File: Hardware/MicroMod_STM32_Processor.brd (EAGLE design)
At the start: 22 x 22 mm, 44 parts, among them J1 MICROMOD-2222, U1 STM32F405RGT6, U3 W25QXX128MBIT-6X5, Y1 12MHz, Y2 32.768kHz

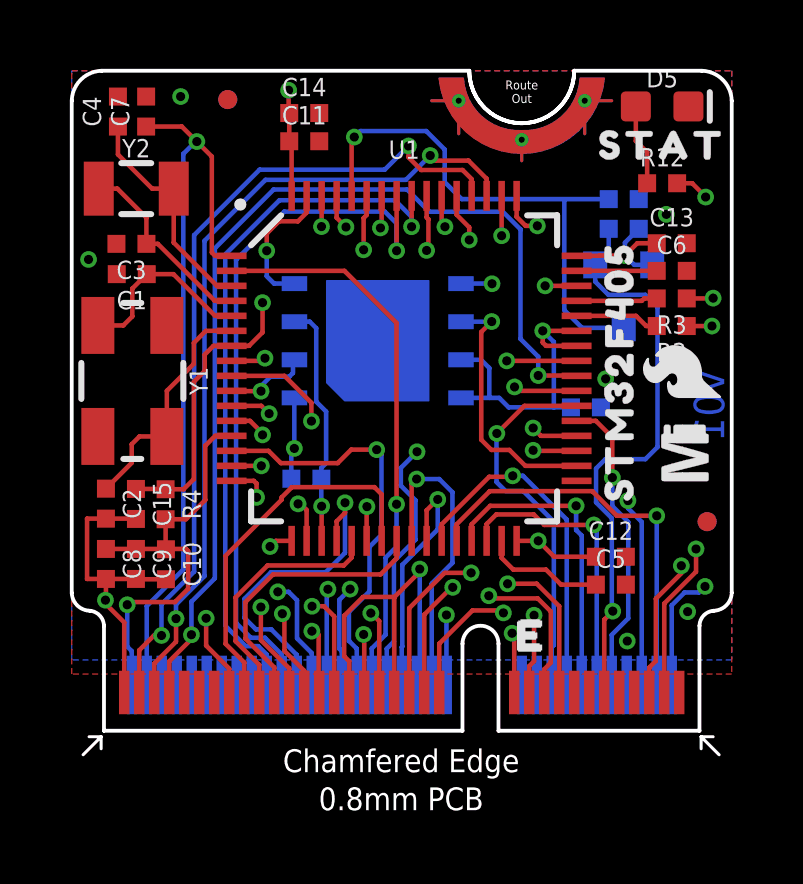
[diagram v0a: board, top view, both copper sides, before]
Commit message: V01 Update
Added jumper for USB host config
Updated crystal caps
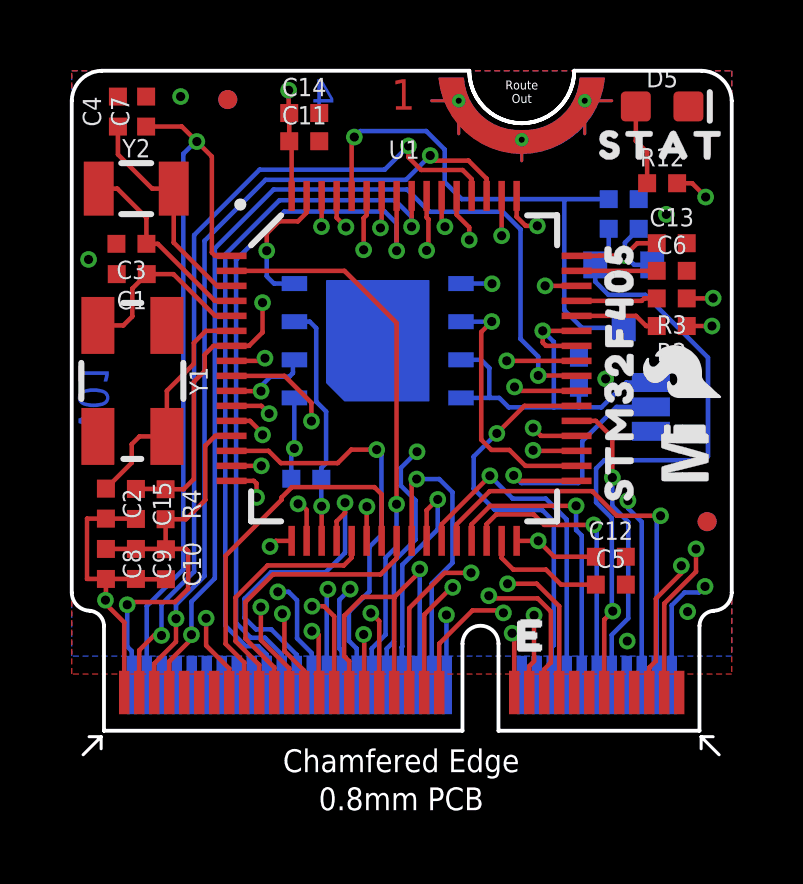
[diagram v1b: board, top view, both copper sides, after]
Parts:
- added HOST_ID: (no value), SparkFun-Jumpers:SMT-JUMPER_3_NO_NO-SILK
- C3, C4: value 22pF -> 15pF
- moved C20 1.18 mm to (16.9, 11.9), turned to 90 degrees
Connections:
- net 3.3V: now also HOST_ID.1
- net GND: now also HOST_ID.3
- net HOST_ID: now also HOST_ID.2
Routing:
- net HOST_ID: track 0.00 -> 8.65 mm, vias 0 -> 1
- net 3.3V: track 49.4 -> 53.1 mm
- net !BOOT: track 19.2 -> 21.8 mm
- net D1: track 12.6 -> 13.8 mm
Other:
- board text added: "1"
- board text added: "2"
- board text added: "3"
- board text added: "4"

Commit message: The 'ol pin switch-a-roo
- Swapped D0/D1 with PWM0/1 - PWM pins weren't capable of PWM
- Swapped BATT_VIN with STAT - BATT_VIN needs to be on an ADC pin
- Moved PB13 to G10 - Based on testing VBUS needs to be broken out or pulled high for USB HS/FS to work correctly
- Moved PB12 from jumper to G11 for USB Host ID to match with SAMD51 MM
- Reorganized G0-G6 for better routing
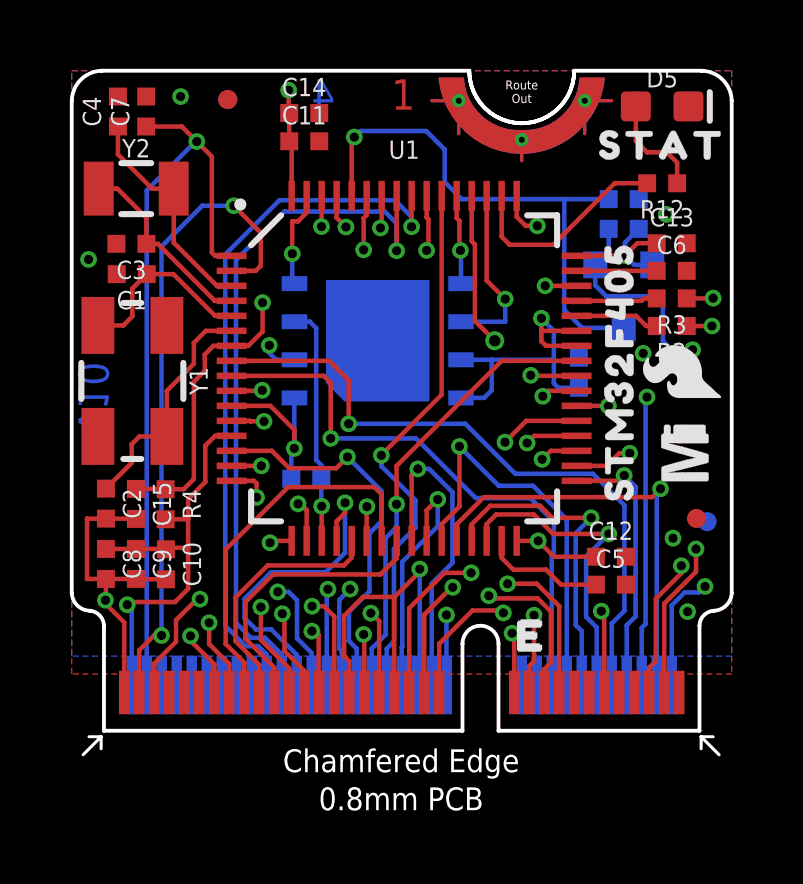
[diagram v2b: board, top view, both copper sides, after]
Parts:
- removed HOST_ID: (no value), SparkFun-Jumpers:SMT-JUMPER_3_NO_NO-SILK
- moved FD1 0.37 mm to (20.8, 7.08)
- moved U$5 0.10 mm to (5.16, 6.36)
- moved U$2 0.07 mm to (12.2, 6.36)
- turned R12 to 180 degrees
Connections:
- removed net G7: J1.69, U1.40
- new net HOST_VBUS: J1.63, U1.34
- net 3.3V: no longer HOST_ID.1
- net BATT_VIN: now also U1.15; no longer U1.50
- net D0: now also U1.8; no longer U1.37
- net D1: now also U1.9; no longer U1.38
- net FLASH_!CS: now also U1.11; no longer U1.39
- net FLASH_SCK: now also U1.51; no longer U1.34
- net FLASH_SDI: now also U1.53; no longer U1.11
- net FLASH_SDO: now also U1.52; no longer U1.10
- net G0: now also U1.54; no longer U1.41
- net G1: now also U1.41; no longer U1.2
- net G3: now also U1.39; no longer U1.53
- net G4: now also U1.40; no longer U1.54
- net G5: now also U1.2; no longer U1.52
- net G6: now also U1.10; no longer U1.51
- net GND: no longer HOST_ID.3
- net HOST_ID: now also J1.8; no longer HOST_ID.2
- net PWM0: now also U1.37; no longer U1.8
- net PWM1: now also U1.38; no longer U1.9
- net STAT: now also U1.50; no longer U1.15
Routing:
- net HOST_VBUS: track 0.00 -> 41.9 mm, vias 0 -> 2
- net G7: track 33.4 -> 0.00 mm, vias 2 -> 0
- net BATT_VIN: track 36.4 -> 14.8 mm
- net STAT: track 23.3 -> 7.17 mm, vias 2 -> 0
- net G6: track 27.2 -> 13.3 mm
- net D0: track 10.1 -> 22.1 mm
- net G3: track 26.3 -> 14.7 mm
- net FLASH_SDI: track 14.3 -> 2.99 mm, vias 2 -> 1
- net FLASH_SDO: track 2.86 -> 13.9 mm, vias 1 -> 2
- net G4: track 25.5 -> 15.5 mm
- net FLASH_!CS: track 13.1 -> 5.78 mm, vias 2 -> 1
- net PWM0: track 18.6 -> 11.8 mm
- net G5: track 27.9 -> 21.7 mm
- net D1: track 13.8 -> 19.3 mm
- net SWCLK: track 22.5 -> 18.2 mm
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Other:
- board text added: "v10"
- board text removed: "v01"

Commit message: V10 design review changes
Removed battery and 3.3V_EN connections to MicroMod
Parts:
- removed C7: 0.1uF, SparkFun-Capacitors:0402-TIGHT
- C15, C8: device SparkFun-Capacitors:0402-TIGHT -> SparkFun-Capacitors:0402
- moved C4 0.82 mm to (1.99, 20.0), turned to 180 degrees
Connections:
- removed net 3V3_EN: J1.4, U1.28
- removed net V_BATT: C7.1, J1.72, U1.1
- net GND: now also U1.28; no longer C7.2
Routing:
- net V_BATT: track 25.4 -> 0.00 mm, vias 1 -> 0
- net 3V3_EN: track 14.4 -> 0.00 mm, vias 1 -> 0
- net G5: track 21.7 -> 18.1 mm
- net GND: track 33.3 -> 35.3 mm
- net BOOT0: track 18.1 -> 17.0 mm
- net D1: track 19.3 -> 18.4 mm
- net D0: track 22.1 -> 21.3 mm
- net A0: track 10.7 -> 9.98 mm
- net N$5: track 7.59 -> 6.91 mm

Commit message: Double-check changes
- Added VDD range
- Updated 0.1uF cap footprints from 0402 to 0402_TIGHT
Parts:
- C15, C8: device SparkFun-Capacitors:0402 -> SparkFun-Capacitors:0402-TIGHT
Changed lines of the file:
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@@
 <attribute name="VALUE" x="7.75" y="20.028" size="0.6096" layer="27" font="vector" ratio="20" align="top-center"/>
 </element>
-<element name="C15" library="SparkFun-Capacitors" package="0402" value="0.1uF" x="2.14" y="7.56" smashed="yes" rot="R270">
+<element name="C15" library="SparkFun-Capacitors" package="0402-TIGHT" value="0.1uF" x="2.14" y="7.56" smashed="yes" rot="R270">
 <attribute name="NAME" x="2.702" y="7.56" size="0.6096" layer="25" font="vector" ratio="20" rot="R270" align="bottom-center"/>
 <attribute name="PROD_ID" value="CAP-15083" x="-44.85" y="-30.54" size="1.778" layer="27" rot="R270" display="off"/>
@@
 <attribute name="VALUE" x="20" y="14.768" size="0.6096" layer="27" font="vector" ratio="20" align="top-center"/>
 </element>
-<element name="C8" library="SparkFun-Capacitors" package="0402" value="0.1uF" x="1.14" y="5.56" smashed="yes" rot="R270">
+<element name="C8" library="SparkFun-Capacitors" package="0402-TIGHT" value="0.1uF" x="1.14" y="5.56" smashed="yes" rot="R270">
 <attribute name="NAME" x="1.702" y="5.56" size="0.6096" layer="25" font="vector" ratio="20" rot="R270" align="bottom-center"/>
 <attribute name="PROD_ID" value="CAP-15083" x="-36.96" y="-49.05" size="1.778" layer="27" rot="R270" display="off"/>
@@
 <contactref element="R4" pad="1"/>
 <wire x1="3.12" y1="8.06" x2="3.13" y2="8.05" width="0.1524" layer="1"/>
-<wire x1="3.12" y1="8.06" x2="2.14" y2="8.14" width="0.1524" layer="1"/>
+<wire x1="3.12" y1="8.06" x2="2.14" y2="8.06" width="0.1524" layer="1"/>
 <wire x1="5.33" y1="12.83" x2="4.7251375" y2="12.83" width="0.1524" layer="1"/>
 <wire x1="4.7251375" y1="12.83" x2="4.4332" y2="12.5380625" width="0.1524" layer="1"/>
@@
 <wire x1="1.75" y1="1.275" x2="1.75" y2="3.61" width="0.1524" layer="1"/>
 <wire x1="1.75" y1="3.61" x2="1.14" y2="4.22" width="0.1524" layer="1"/>
-<wire x1="1.14" y1="4.22" x2="1.14" y2="4.98" width="0.1524" layer="1"/>
+<wire x1="1.14" y1="4.22" x2="1.14" y2="5.06" width="0.1524" layer="1"/>
 <wire x1="2.14" y1="5.06" x2="2.15" y2="5.05" width="0.1524" layer="1"/>
 <wire x1="3.14" y1="5.05" x2="2.15" y2="5.05" width="0.1524" layer="1"/>
-<wire x1="2.14" y1="5.06" x2="1.14" y2="4.98" width="0.1524" layer="1"/>
-<wire x1="2.14" y1="6.98" x2="2.13" y2="7.07" width="0.1524" layer="1"/>
+<wire x1="2.14" y1="5.06" x2="1.14" y2="5.06" width="0.1524" layer="1"/>
+<wire x1="2.14" y1="7.06" x2="2.13" y2="7.07" width="0.1524" layer="1"/>
 <wire x1="2.13" y1="7.07" x2="1.14" y2="7.07" width="0.1524" layer="1"/>
 <wire x1="1.14" y1="7.07" x2="0.51" y2="7.07" width="0.1524" layer="1"/>
-<wire x1="1.14" y1="4.98" x2="0.51" y2="5.06" width="0.1524" layer="1"/>
+<wire x1="1.14" y1="5.06" x2="0.51" y2="5.06" width="0.1524" layer="1"/>
 <wire x1="0.51" y1="5.06" x2="0.51" y2="7.07" width="0.1524" layer="1"/>
 <via x="20.53" y="3.97" extent="1-16" drill="0.3048"/>
@@
 <wire x1="12.103" y1="5.603" x2="11.89" y2="5.39" width="0.2" layer="1"/>
 <wire x1="12.661025" y1="5.603" x2="12.103" y2="5.603" width="0.2" layer="1"/>
-<wire x1="17.1" y1="21" x2="20.557" y2="20.81" width="0" layer="19" extent="1-1"/>
-<wire x1="15" y1="19.7" x2="17.1" y2="21" width="0" layer="19" extent="1-1"/>
-<wire x1="12.9" y1="21" x2="15" y2="19.7" width="0" layer="19" extent="1-1"/>
-<wire x1="18.9" y1="17.72" x2="20.557" y2="20.81" width="0" layer="19" extent="1-16"/>
-<wire x1="19.82" y1="17.2126" x2="18.9" y2="17.72" width="0" layer="19" extent="16-16"/>
-<wire x1="20.5" y1="16.25" x2="19.82" y2="17.2126" width="0" layer="19" extent="1-1"/>
-<wire x1="20.5" y1="15.33" x2="20.5" y2="16.25" width="0" layer="19" extent="1-1"/>
-<wire x1="19.0474" y1="12.58" x2="20.5" y2="15.33" width="0" layer="19" extent="1-1"/>
-<wire x1="16.906" y1="12.433" x2="19.0474" y2="12.58" width="0" layer="19" extent="16-16"/>
-<wire x1="8.25" y1="20.59" x2="12.9" y2="21" width="0" layer="19" extent="1-1"/>
-<wire x1="8.25" y1="19.65" x2="8.25" y2="20.59" width="0" layer="19" extent="1-1"/>
-<wire x1="7.83" y1="17.83" x2="8.25" y2="19.65" width="0" layer="19" extent="1-1"/>
-<wire x1="3.63" y1="21.14" x2="8.25" y2="20.59" width="0" layer="19" extent="1-1"/>
-<wire x1="1.49" y1="19.955" x2="3.63" y2="21.14" width="0" layer="19" extent="1-1"/>
-<wire x1="1.49" y1="16.23" x2="1.49" y2="19.955" width="0" layer="19" extent="1-1"/>
-<wire x1="1.5" y1="15.22" x2="1.49" y2="16.23" width="0" layer="19" extent="1-1"/>
-<wire x1="0.56" y1="15.71" x2="1.49" y2="16.23" width="0" layer="19" extent="1-1"/>
-<wire x1="6.41" y1="10.3126" x2="7.425" y2="14.905" width="0" layer="19" extent="16-16"/>
-<wire x1="7.5442" y1="7.5626" x2="6.41" y2="10.3126" width="0" layer="19" extent="1-1"/>
-<wire x1="11.6" y1="5.39" x2="7.83" y2="6.33" width="0" layer="19" extent="1-1"/>
-<wire x1="12.25" y1="1.275" x2="11.5" y2="1.525" width="0" layer="19" extent="1-16"/>
-<wire x1="18.47" y1="4.87" x2="14.38873125" y2="3.9286" width="0" layer="19" extent="1-1"/>
-<wire x1="18.47" y1="5.8" x2="18.47" y2="4.87" width="0" layer="19" extent="1-1"/>
-<wire x1="20.0414" y1="6.419" x2="18.47" y2="5.8" width="0" layer="19" extent="1-1"/>
-<wire x1="20.53" y1="3.97" x2="18.47" y2="4.87" width="0" layer="19" extent="1-1"/>
-<wire x1="20.25" y1="1.275" x2="20.53" y2="3.97" width="0" layer="19" extent="1-1"/>
-<wire x1="18.75" y1="1.275" x2="20.25" y2="1.275" width="0" layer="19" extent="1-1"/>
-<wire x1="2.14" y1="6.98" x2="5.33" y2="10.33" width="0" layer="19" extent="1-1"/>
-<wire x1="1.1242" y1="4.3526" x2="1.14" y2="4.98" width="0" layer="19" extent="1-1"/>
 </signal>
 <signal name="3.3V">
@@
 <contactref element="C10" pad="1"/>
 <wire x1="3.24" y1="6.05" x2="3.14" y2="6.05" width="0.1524" layer="1"/>
-<wire x1="1.14" y1="6.14" x2="2.14" y2="6.06" width="0.1524" layer="1"/>
+<wire x1="1.14" y1="6.06" x2="2.14" y2="6.06" width="0.1524" layer="1"/>
 <wire x1="2.14" y1="6.06" x2="3.13" y2="6.06" width="0.1524" layer="1"/>
 <wire x1="3.13" y1="6.06" x2="3.14" y2="6.05" width="0.1524" layer="1"/>
@@
 <wire x1="16.471" y1="11.433" x2="16.07" y2="11.834" width="0.1524" layer="16"/>
 <wire x1="16.83" y1="13.33" x2="15.656" y2="13.33" width="0.1524" layer="1"/>
-<wire x1="15.6535" y1="13.748" x2="16.83" y2="15.83" width="0" layer="19" extent="1-1"/>
-<wire x1="14.83" y1="6.33" x2="12.975" y2="11.095" width="0" layer="19" extent="1-16"/>
-<wire x1="21.11" y1="4.81" x2="17.47" y2="5.8" width="0" layer="19" extent="1-1"/>
-<wire x1="8.32" y1="8.4" x2="12.975" y2="11.095" width="0" layer="19" extent="16-16"/>
-<wire x1="5.33" y1="9.83" x2="8.32" y2="8.4" width="0" layer="19" extent="1-16"/>
-<wire x1="7.33" y1="17.83" x2="7.425" y2="13.635" width="0" layer="19" extent="1-16"/>
 </signal>
 <signal name="FLASH_SDI">

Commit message: Updated BOM
Replaced 22 ohm resistors with 0 ohm
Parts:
- R2, R3: value 22 -> 0
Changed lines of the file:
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@@
 <?xml version="1.0" encoding="utf-8"?>
 <!DOCTYPE eagle SYSTEM "eagle.dtd">
-<eagle version="9.6.2">
+<eagle version="9.5.2">
 <drawing>
 <settings>
@@
 <setting verticaltext="up"/>
 </settings>
-<grid distance="0.05" unitdist="inch" unit="inch" style="lines" multiple="1" display="yes" altdistance="0.005" altunitdist="inch" altunit="inch"/>
+<grid distance="0.05" unitdist="inch" unit="mm" style="lines" multiple="1" display="yes" altdistance="0.005" altunitdist="inch" altunit="mm"/>
 <layers>
 <layer number="1" name="Top" color="4" fill="1" visible="yes" active="yes"/>
@@
 <attribute name="VALUE" x="19.68" y="18.812" size="0.6096" layer="27" font="vector" ratio="20" rot="R180" align="top-center"/>
 </element>
-<element name="R2" library="SparkFun-Resistors" package="0402-TIGHT" value="22" x="20" y="13.49" smashed="yes" rot="R180">
+<element name="R2" library="SparkFun-Resistors" package="0402-TIGHT" value="0" x="20" y="13.49" smashed="yes" rot="R180">
 <attribute name="NAME" x="20" y="12.928" size="0.6096" layer="25" font="vector" ratio="20" rot="R180" align="bottom-center"/>
-<attribute name="PROD_ID" value="RES-12427" x="3.49" y="64.29" size="1.778" layer="27" rot="R180" display="off"/>
-<attribute name="VALUE" value="22" x="20" y="14.052" size="0.6096" layer="27" font="vector" ratio="20" rot="R180" align="top-center"/>
-</element>
-<element name="R3" library="SparkFun-Resistors" package="0402-TIGHT" value="22" x="20" y="14.41" smashed="yes" rot="R180">
+<attribute name="PROD_ID" value="RES-14244" x="3.49" y="64.29" size="1.778" layer="27" rot="R180" display="off"/>
+<attribute name="VALUE" value="0" x="20" y="13.49" size="1.778" layer="27" rot="R180" display="off"/>
+</element>
+<element name="R3" library="SparkFun-Resistors" package="0402-TIGHT" value="0" x="20" y="14.41" smashed="yes" rot="R180">
 <attribute name="NAME" x="20" y="13.848" size="0.6096" layer="25" font="vector" ratio="20" rot="R180" align="bottom-center"/>
-<attribute name="PROD_ID" value="RES-12427" x="0.95" y="65.21" size="1.778" layer="27" rot="R180" display="off"/>
-<attribute name="VALUE" value="22" x="20" y="14.972" size="0.6096" layer="27" font="vector" ratio="20" rot="R180" align="top-center"/>
+<attribute name="PROD_ID" value="RES-14244" x="0.95" y="65.21" size="1.778" layer="27" rot="R180" display="off"/>
+<attribute name="VALUE" value="0" x="20" y="14.41" size="1.778" layer="27" rot="R180" display="off"/>
 </element>
 <element name="R4" library="SparkFun-Resistors" package="0402-TIGHT" value="5.1k" x="3.13" y="7.55" smashed="yes" rot="R270">

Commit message: Updated USB Load resistors
Replaced 0 ohm resistors with 22 ohm
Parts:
- R2, R3: value 0 -> 22
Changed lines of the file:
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@@
 <?xml version="1.0" encoding="utf-8"?>
 <!DOCTYPE eagle SYSTEM "eagle.dtd">
-<eagle version="9.5.2">
+<eagle version="9.6.2">
 <drawing>
 <settings>
@@
 <setting verticaltext="up"/>
 </settings>
-<grid distance="0.05" unitdist="inch" unit="mm" style="lines" multiple="1" display="yes" altdistance="0.005" altunitdist="inch" altunit="mm"/>
+<grid distance="0.05" unitdist="inch" unit="inch" style="lines" multiple="1" display="yes" altdistance="0.005" altunitdist="inch" altunit="inch"/>
 <layers>
 <layer number="1" name="Top" color="4" fill="1" visible="yes" active="yes"/>
@@
 <attribute name="VALUE" x="19.68" y="18.812" size="0.6096" layer="27" font="vector" ratio="20" rot="R180" align="top-center"/>
 </element>
-<element name="R2" library="SparkFun-Resistors" package="0402-TIGHT" value="0" x="20" y="13.49" smashed="yes" rot="R180">
+<element name="R2" library="SparkFun-Resistors" package="0402-TIGHT" value="22" x="20" y="13.49" smashed="yes" rot="R180">
 <attribute name="NAME" x="20" y="12.928" size="0.6096" layer="25" font="vector" ratio="20" rot="R180" align="bottom-center"/>
-<attribute name="PROD_ID" value="RES-14244" x="3.49" y="64.29" size="1.778" layer="27" rot="R180" display="off"/>
-<attribute name="VALUE" value="0" x="20" y="13.49" size="1.778" layer="27" rot="R180" display="off"/>
-</element>
-<element name="R3" library="SparkFun-Resistors" package="0402-TIGHT" value="0" x="20" y="14.41" smashed="yes" rot="R180">
+<attribute name="PROD_ID" value="RES-12427" x="3.49" y="64.29" size="1.778" layer="27" rot="R180" display="off"/>
+</element>
+<element name="R3" library="SparkFun-Resistors" package="0402-TIGHT" value="22" x="20" y="14.41" smashed="yes" rot="R180">
 <attribute name="NAME" x="20" y="13.848" size="0.6096" layer="25" font="vector" ratio="20" rot="R180" align="bottom-center"/>
-<attribute name="PROD_ID" value="RES-14244" x="0.95" y="65.21" size="1.778" layer="27" rot="R180" display="off"/>
-<attribute name="VALUE" value="0" x="20" y="14.41" size="1.778" layer="27" rot="R180" display="off"/>
+<attribute name="PROD_ID" value="RES-12427" x="0.95" y="65.21" size="1.778" layer="27" rot="R180" display="off"/>
 </element>
 <element name="R4" library="SparkFun-Resistors" package="0402-TIGHT" value="5.1k" x="3.13" y="7.55" smashed="yes" rot="R270">

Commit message: Swap USART2 for USART1, connect USART2 to ground.
Also renamed COPI/CIPO to POCI/PICO to match new naming conventions.
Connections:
- net CIPO renamed POCI
- net COPI renamed PICO
- net 3.3V: no longer U1.42, U1.43
- net GND: now also U1.16, U1.17
- net RX1: now also U1.43; no longer U1.17
- net TX1: now also U1.42; no longer U1.16
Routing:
- net 3.3V: track 49.7 -> 47.5 mm
- net TX1: track 16.6 -> 15.9 mm
- net RX1: track 14.7 -> 14.0 mm
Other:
- board text added: "Revised by: Alex Brudner"

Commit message: Rerouted board, cleaned up schematic.
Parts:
- added TP1, TP2, TP3, TP4: TEST-POINTTP_15TH_THRU, SparkFun-Connectors:TP_15TH
- moved LOGO2 11.6 mm to (15.5, 16.8)
- moved C12 1.13 mm to (16.9, 5.68)
- moved C5 1.12 mm to (16.9, 4.77)
- moved U$3 0.20 mm to (20.6, 9.23)
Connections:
- net !RESET: now also TP4.1
- net BOOT0: now also TP3.1
- net RX1: now also TP1.1
- net TX1: now also TP2.1
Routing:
- net RX1: track 14.0 -> 16.3 mm, vias 2 -> 0
- net !RESET: track 35.5 -> 37.3 mm, vias 2 -> 1
- net HOST_VBUS: track 42.0 -> 43.4 mm
- net 3.3V: track 47.5 -> 48.7 mm
- net TX1: track 15.9 -> 14.8 mm, vias 2 -> 1
- net N$46: track 4.08 -> 3.12 mm
- net BOOT0: vias 1 -> 0
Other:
- board text added: "v20"
- board text removed: "v10"
